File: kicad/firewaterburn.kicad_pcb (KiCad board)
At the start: 2 copper layers, 105.2 x 79 mm, 85 parts, among them J1 AudioJack2_SwitchT, J2 AudioJack2_SwitchT, J3 Conn_01x03, J4 AudioJack2_SwitchT, J5 AudioJack2_SwitchT, J6 AudioJack2_SwitchT, J7 AudioJack2_SwitchT, J8 R61529 LCD, P1 USB_C_Plug_USB2.0, Q1 DMN61D9UWQ-13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

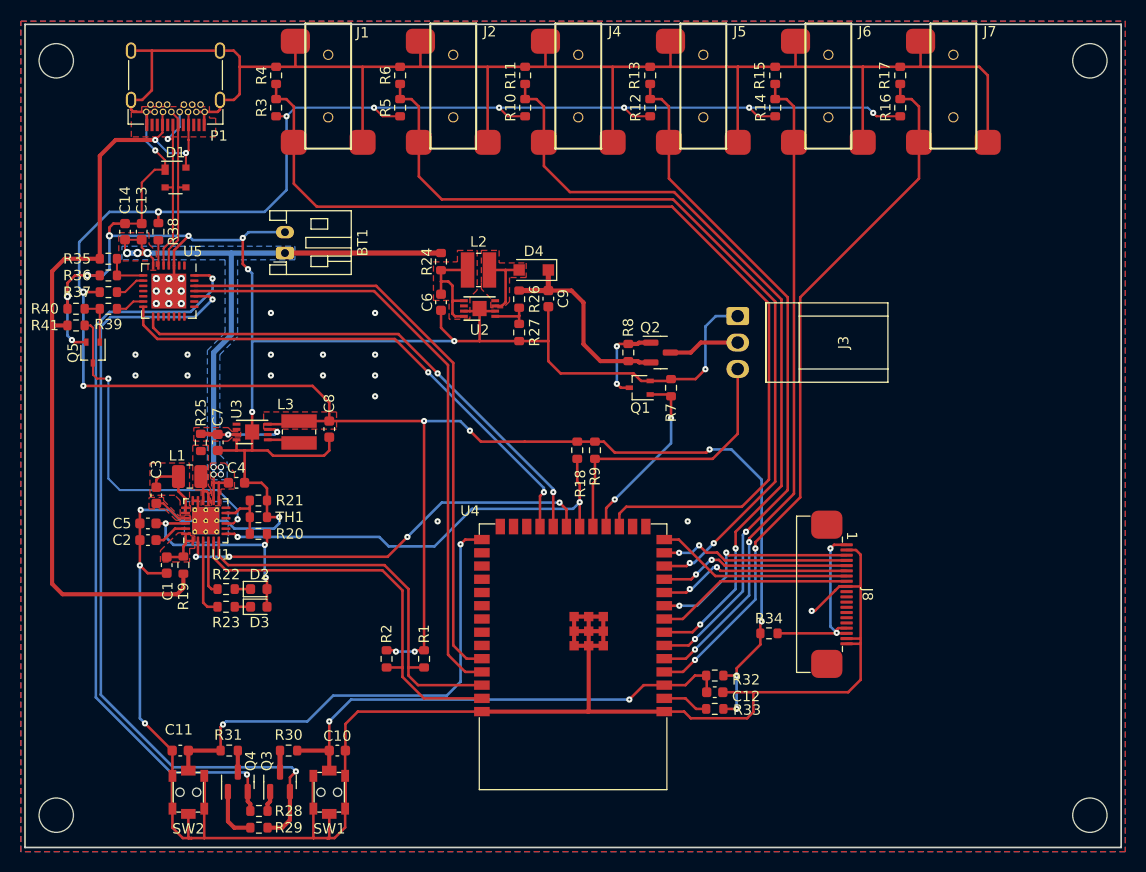
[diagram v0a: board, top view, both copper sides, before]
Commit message: remove Rx with 0 Ohms
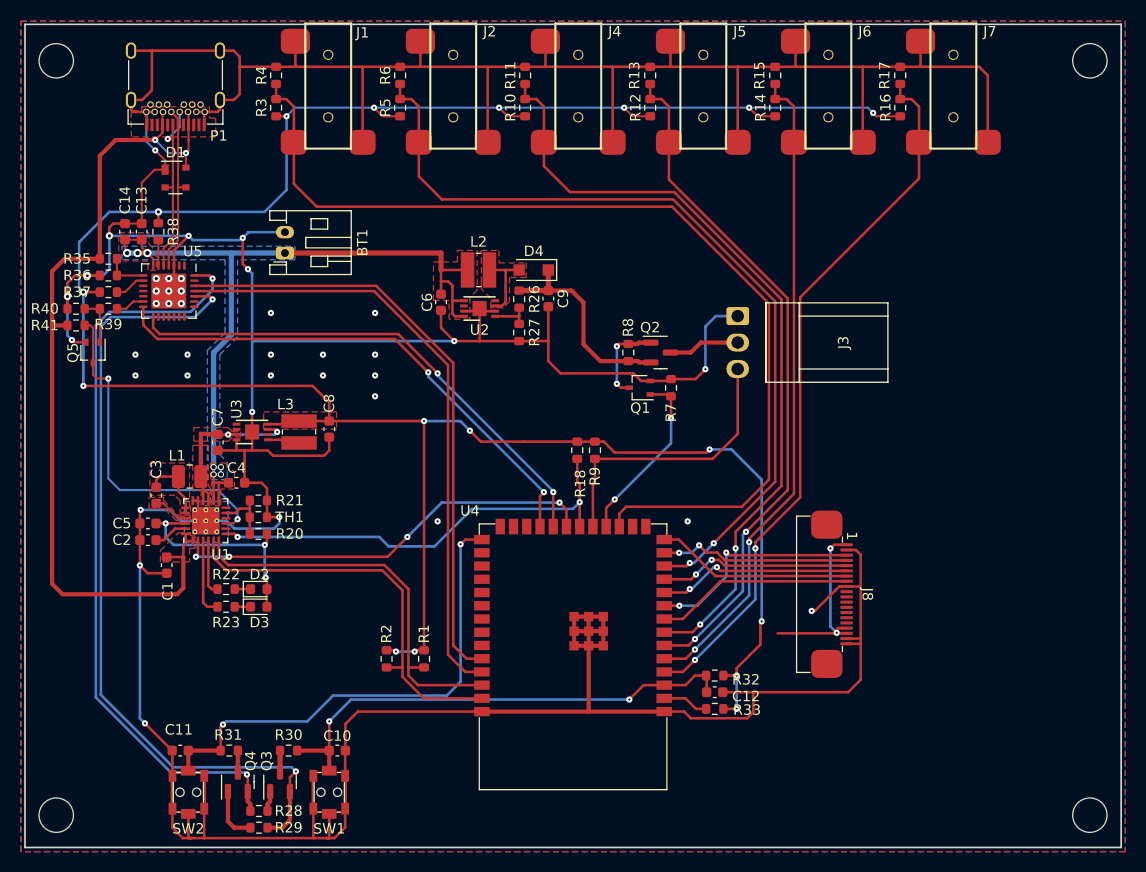
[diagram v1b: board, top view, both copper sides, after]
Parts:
- removed R19, R24, R25, R34: 0R, Resistor_SMD:R_0603_1608Metric
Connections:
- C1 pad 1: Net-(C1-Pad1) -> VBUS
- C6 pad 1: Net-(C6-Pad1) -> VAA
- C7 pad 1: Net-(C7-Pad1) -> VS
- J8 pad 1: Net-(J8-Pad1) -> +3V3
- J8 pad 17: Net-(J8-Pad1) -> +3V3
- J8 pad 18: Net-(J8-Pad1) -> +3V3
- L2 pad 1: Net-(C6-Pad1) -> VAA
- U1 pad 1: Net-(C1-Pad1) -> VBUS
- U1 pad 24: Net-(C1-Pad1) -> VBUS
- U2 pad 5: Net-(C6-Pad1) -> VAA
- U2 pad 8: Net-(C6-Pad1) -> VAA
- U3 pad 3: Net-(C7-Pad1) -> VS
- U3 pad 7: Net-(C7-Pad1) -> VS
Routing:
- net +3V3: track 245.0 -> 263.1 mm, vias 17 -> 19
- net Net-(J8-Pad1): track 18.1 -> 0.00 mm, vias 2 -> 0
- net VS: track 3.70 -> 17.0 mm, vias 0 -> 2
- net VAA: track 65.7 -> 78.5 mm
- net Net-(C6-Pad1): track 11.2 -> 0.00 mm
- net Net-(C7-Pad1): track 9.23 -> 0.00 mm, vias 2 -> 0
- net VBUS: track 79.0 -> 85.2 mm
- net Net-(C1-Pad1): track 4.58 -> 0.00 mm
- added copper zone on F.Cu, net VBUS
- removed copper zone on F.Cu, net Net-(C1-Pad1)
- removed copper zone on F.Cu, net Net-(C6-Pad1)
- removed copper zone on F.Cu, net Net-(C7-Pad1)
